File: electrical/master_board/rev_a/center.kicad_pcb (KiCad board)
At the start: 2 copper layers, 0 parts

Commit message: Inject the PCB outlines into master/center/ne/nw/se/sw PCB's.
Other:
- board outline added: 125 x 97.6 mm

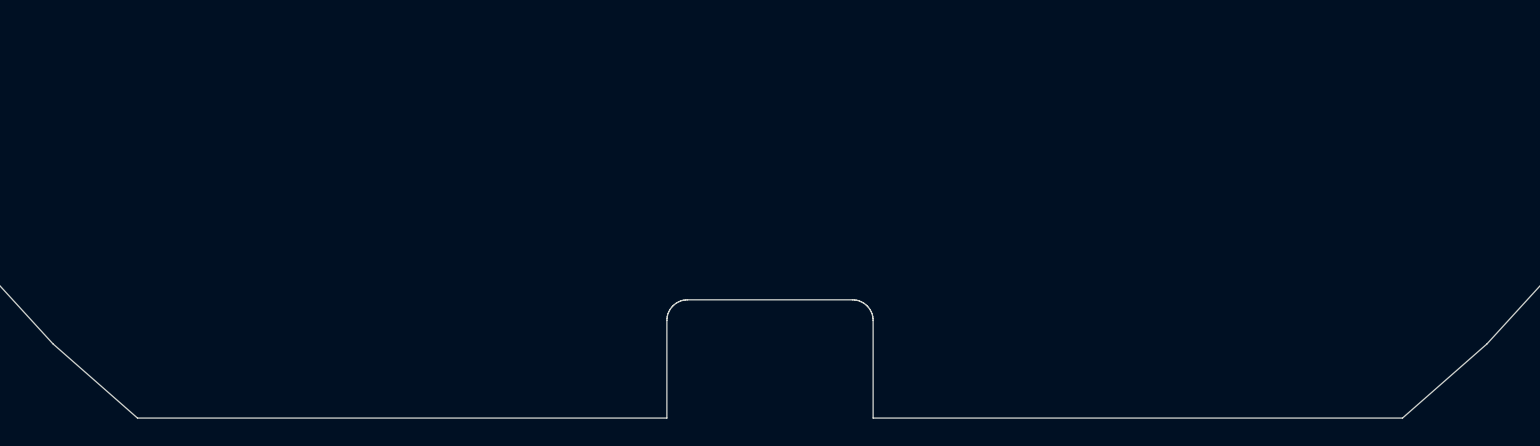
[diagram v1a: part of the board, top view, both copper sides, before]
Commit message: Updated some of the schematics and PCB's via hr2_models.py .
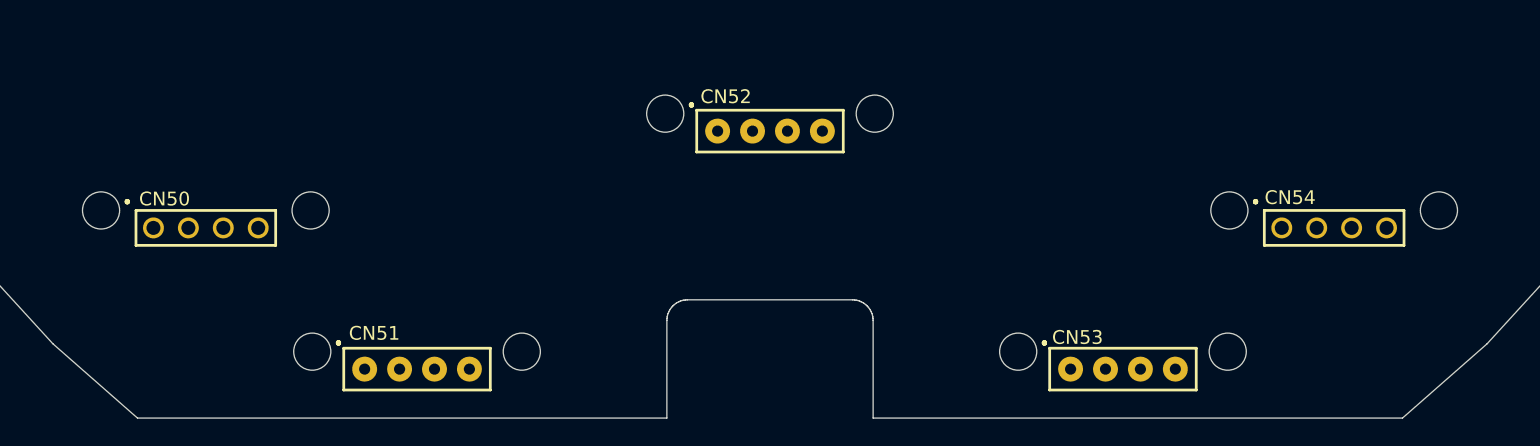
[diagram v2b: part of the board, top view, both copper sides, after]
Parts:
- added CN50: HCSR04;F1X4, HR2:HCSR04_F1x4_MATE, F.Cu at (59.0, 144.8)
- added CN51: HCSR04LP;F1X4, HR2:HCSR04_F1x4LP_MATE, F.Cu at (74.3, 155.0)
- added CN52: HCSR04LP;F1X4, HR2:HCSR04_F1x4LP_MATE, F.Cu at (100.0, 137.7)
- added CN53: HCSR04LP;F1X4, HR2:HCSR04_F1x4LP_MATE, F.Cu at (125.7, 155.0)
- added CN54: HCSR04;F1X4, HR2:HCSR04_F1x4_MATE, F.Cu at (141.0, 144.8)

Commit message: Successfully placed a font surface non-rotated footprint in ne.kicad_pcb.
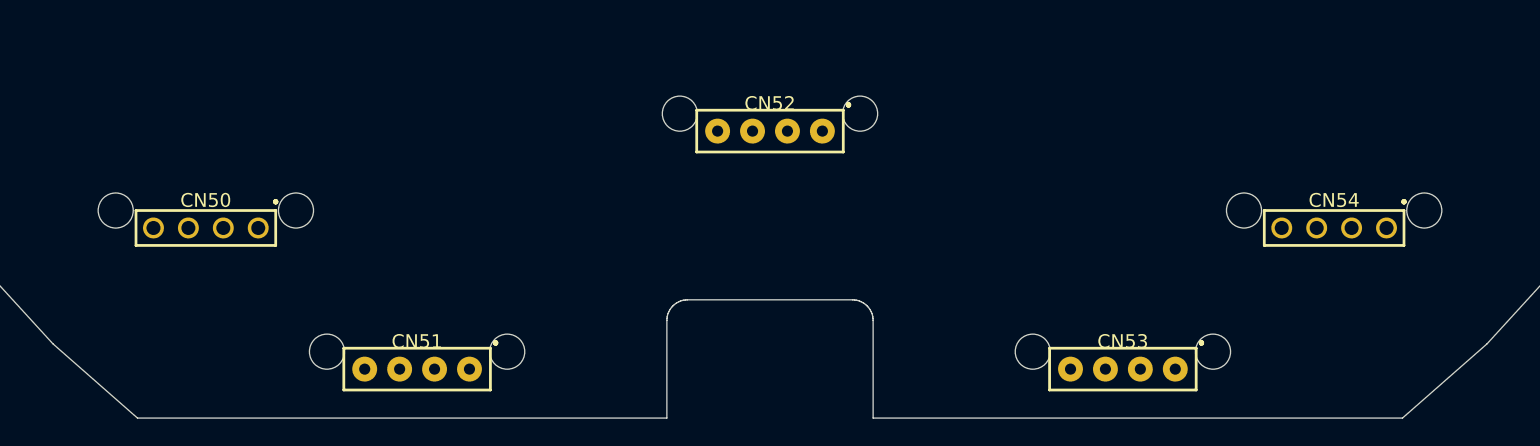
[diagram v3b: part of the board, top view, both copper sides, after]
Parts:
- CN50: value HCSR04;F1X4 -> HCSR04;F1x4; footprint HR2:HCSR04_F1x4_MATE -> HR2:HCSR04_F1x4
- CN51, CN53: value HCSR04LP;F1X4 -> HCSR04;F1x4LP; footprint HR2:HCSR04_F1x4LP_MATE -> HR2:HCSR04_F1x4LP; moved to B.Cu
- CN52: value HCSR04LP;F1X4 -> HCSR04;F1x4LP; footprint HR2:HCSR04_F1x4LP_MATE -> HR2:HCSR04_F1x4LP
- CN54: value HCSR04;F1X4 -> HCSR04;F1x4H; footprint HR2:HCSR04_F1x4_MATE -> HR2:HCSR04_F1x4H

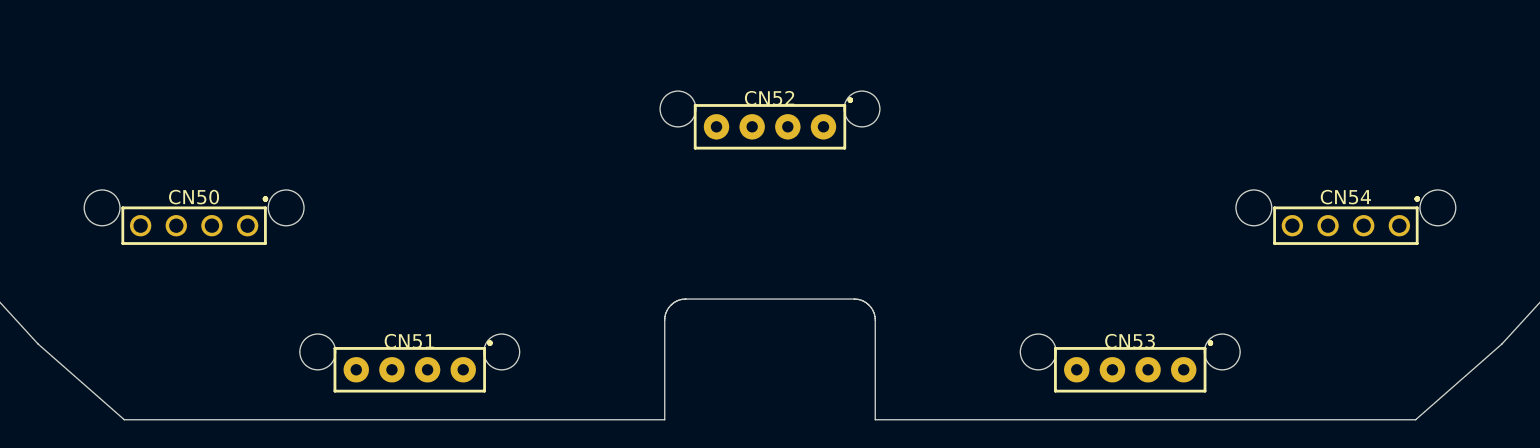
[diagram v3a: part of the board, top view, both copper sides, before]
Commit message: Finally sonars placed.  Had to manually specify the rotattions thought.
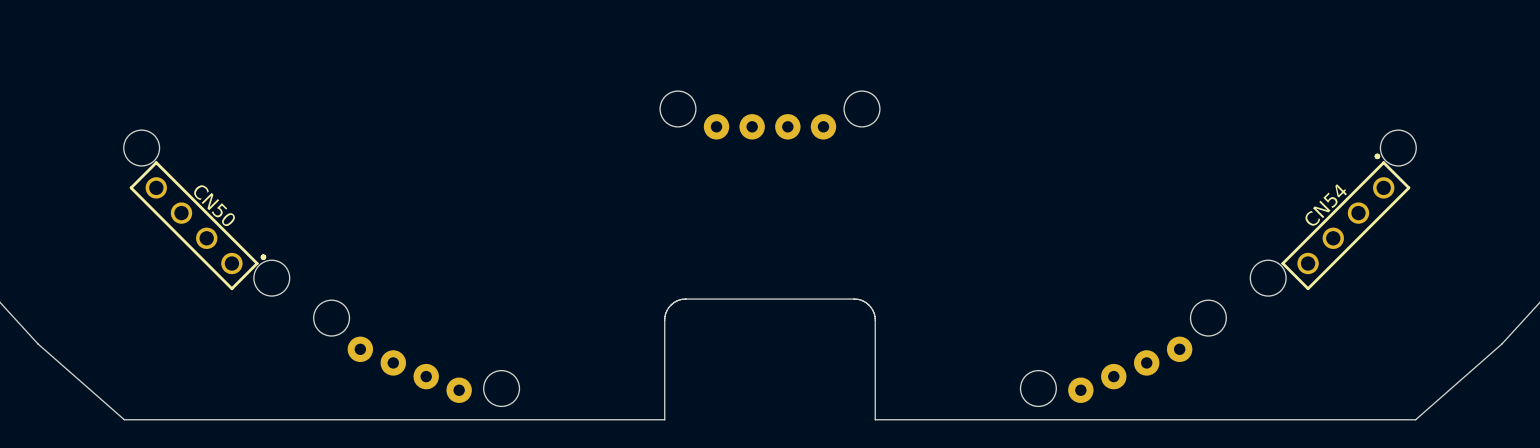
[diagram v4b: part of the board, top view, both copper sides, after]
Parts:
- CN52: moved to B.Cu
- turned CN50 to 315 degrees
- turned CN51 to 157.5 degrees
- turned CN52 to 180 degrees
- turned CN53 to 202.5 degrees
- turned CN54 to 45 degrees

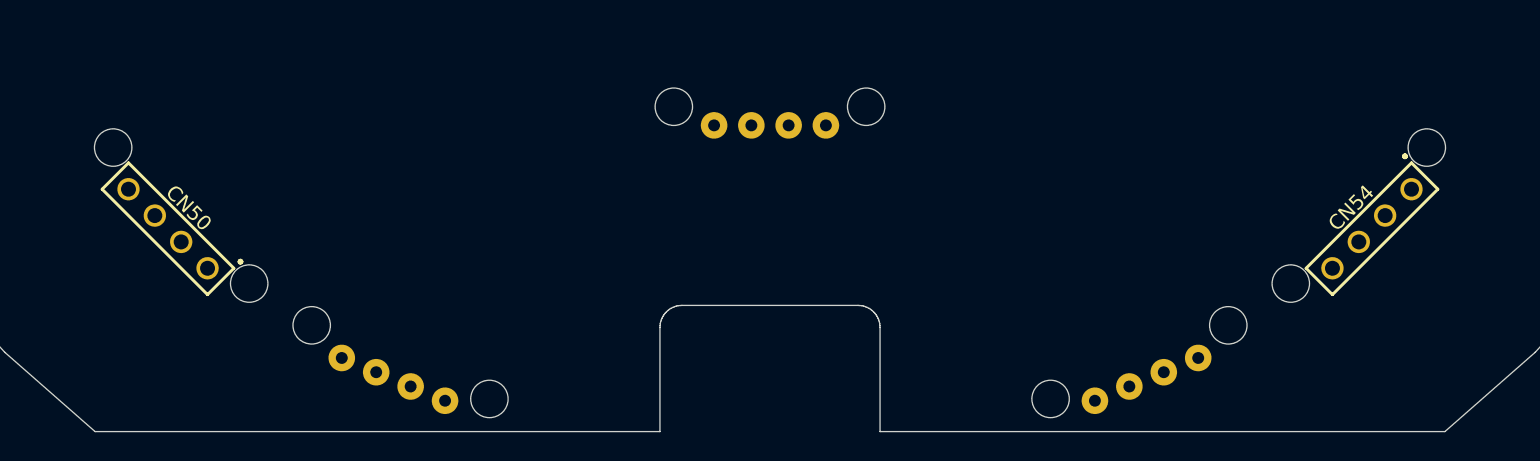
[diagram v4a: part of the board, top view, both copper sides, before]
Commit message: The PCBChunk'ification of Sonars is complete.
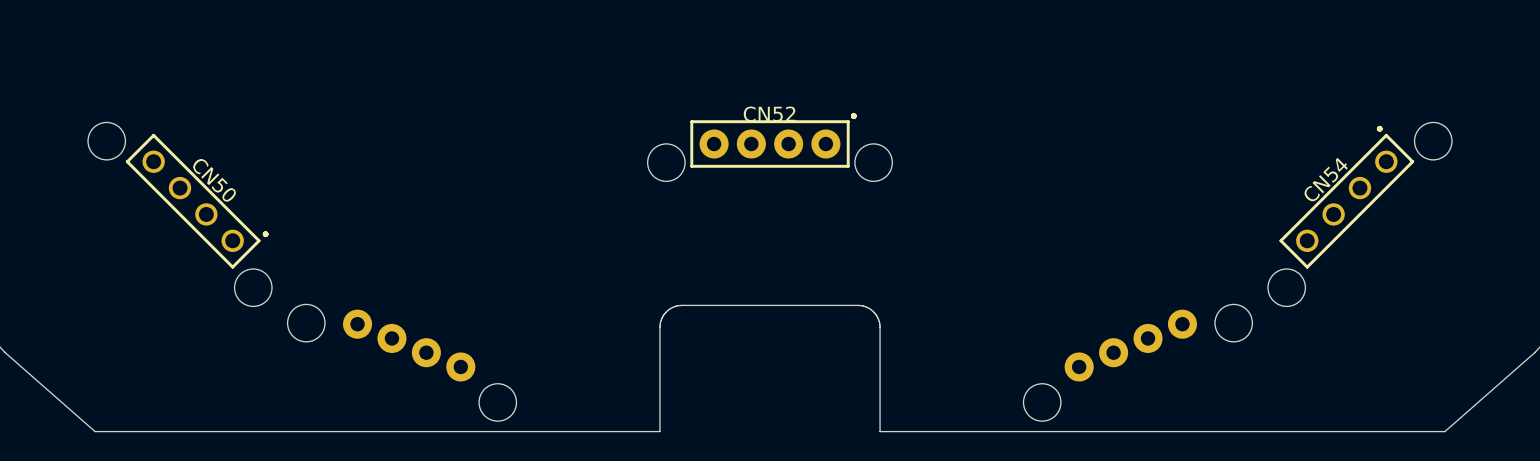
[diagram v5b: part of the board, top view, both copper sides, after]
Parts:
- CN50: value HCSR04;F1x4 -> HCSR04;F1X4
- CN51, CN53: value HCSR04;F1x4LP -> HCSR04LP;F1X4
- CN52: value HCSR04;F1x4LP -> HCSR04LP;F1X4; moved to F.Cu
- CN54: value HCSR04;F1x4H -> HCSR04;F1X4; footprint HR2:HCSR04_F1x4H -> HR2:HCSR04_F1x4
- moved CN54 2.54 mm to (139.3, 142.9)
- moved CN50 2.54 mm to (60.7, 142.9)
- moved CN51 2.54 mm to (75.4, 152.7)
- moved CN53 2.54 mm to (124.6, 152.7)
- moved CN52 1.27 mm to (100.0, 139.0), turned to 0 degrees

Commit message: Got Encoder PCB's installed on the center PCB.
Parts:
- added CN55: HR2_EncoderMate;2XF1X3, HR2:ENCODER_MATE, F.Cu at (136.0, 100.0)
- added CN56: HR2_EncoderMate;2XF1X3, HR2:ENCODER_MATE, F.Cu at (64.0, 100.0)
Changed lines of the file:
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@@
     (tracks 0)
     (zones 0)
-    (modules 5)
+    (modules 7)
     (nets 1)
   )
@@
     (add_net "Net-(CN54-Pad3)")
     (add_net "Net-(CN54-Pad4)")
+    (add_net "Net-(CN55-Pad1)")
+    (add_net "Net-(CN55-Pad2)")
+    (add_net "Net-(CN55-Pad3)")
+    (add_net "Net-(CN55-Pad4)")
+    (add_net "Net-(CN55-Pad5)")
+    (add_net "Net-(CN55-Pad6)")
+    (add_net "Net-(CN56-Pad1)")
+    (add_net "Net-(CN56-Pad2)")
+    (add_net "Net-(CN56-Pad3)")
+    (add_net "Net-(CN56-Pad4)")
+    (add_net "Net-(CN56-Pad5)")
+    (add_net "Net-(CN56-Pad6)")
+  )
+  (module HR2:ENCODER_MATE (layer F.Cu)
+    (at 136 100 180)
+    (fp_text reference CN55 (at 0 -2) (layer F.SilkS)
+      (effects (font (size 1 1) (thickness 0.2)))
+    )
+    (fp_text value HR2_EncoderMate;2XF1X3 (at 0 0) (layer F.Fab)
+      (effects (font (size 1 1) (thickness 0.2)))
+    )
+    (fp_line (start -1.27 -13.84) (end -1.27 -21.46) (layer F.SilkS) (width 0.2))
+    (fp_line (start 1.27 -13.84) (end -1.27 -13.84) (layer F.SilkS) (width 0.2))
+    (fp_line (start 1.27 -21.46) (end 1.27 -13.84) (layer F.SilkS) (width 0.2))
+    (fp_line (start -1.27 -21.46) (end 1.27 -21.46) (layer F.SilkS) (width 0.2))
+    (fp_line (start -1.83 -13.91) (end -1.91 -13.94) (layer F.SilkS) (width 0.2))
+    (fp_line (start -1.81 -13.84) (end -1.83 -13.91) (layer F.SilkS) (width 0.2))
+    (fp_line (start -1.83 -13.77) (end -1.81 -13.84) (layer F.SilkS) (width 0.2))
+    (fp_line (start -1.91 -13.74) (end -1.83 -13.77) (layer F.SilkS) (width 0.2))
+    (fp_line (start -1.98 -13.77) (end -1.91 -13.74) (layer F.SilkS) (width 0.2))
+    (fp_line (start -2.01 -13.84) (end -1.98 -13.77) (layer F.SilkS) (width 0.2))
+    (fp_line (start -1.98 -13.91) (end -2.01 -13.84) (layer F.SilkS) (width 0.2))
+    (fp_line (start -1.91 -13.94) (end -1.98 -13.91) (layer F.SilkS) (width 0.2))
+    (fp_line (start -1.27 21.46) (end -1.27 13.84) (layer F.SilkS) (width 0.2))
+    (fp_line (start 1.27 21.46) (end -1.27 21.46) (layer F.SilkS) (width 0.2))
+    (fp_line (start 1.27 13.84) (end 1.27 21.46) (layer F.SilkS) (width 0.2))
+    (fp_line (start -1.27 13.84) (end 1.27 13.84) (layer F.SilkS) (width 0.2))
+    (fp_line (start -1.83 21.39) (end -1.91 21.36) (layer F.SilkS) (width 0.2))
+    (fp_line (start -1.81 21.46) (end -1.83 21.39) (layer F.SilkS) (width 0.2))
+    (fp_line (start -1.83 21.53) (end -1.81 21.46) (layer F.SilkS) (width 0.2))
+    (fp_line (start -1.91 21.56) (end -1.83 21.53) (layer F.SilkS) (width 0.2))
+    (fp_line (start -1.98 21.53) (end -1.91 21.56) (layer F.SilkS) (width 0.2))
+    (fp_line (start -2.01 21.46) (end -1.98 21.53) (layer F.SilkS) (width 0.2))
+    (fp_line (start -1.98 21.39) (end -2.01 21.46) (layer F.SilkS) (width 0.2))
+    (fp_line (start -1.91 21.36) (end -1.98 21.39) (layer F.SilkS) (width 0.2))
+    (pad 3 thru_hole circle (at 0 15.11 180) (size 1.52 1.52) (drill 1.02) (layers *.Cu *.Mask))
+    (pad 2 thru_hole circle (at 0 17.65 180) (size 1.52 1.52) (drill 1.02) (layers *.Cu *.Mask))
+    (pad 1 thru_hole circle (at 0 20.19 180) (size 1.52 1.52) (drill 1.02) (layers *.Cu *.Mask))
+    (pad 6 thru_hole circle (at 0 -20.19 180) (size 1.52 1.52) (drill 1.02) (layers *.Cu *.Mask))
+    (pad 5 thru_hole circle (at 0 -17.65 180) (size 1.52 1.52) (drill 1.02) (layers *.Cu *.Mask))
+    (pad 4 thru_hole circle (at 0 -15.11 180) (size 1.52 1.52) (drill 1.02) (layers *.Cu *.Mask))
+  )
+  (module HR2:ENCODER_MATE (layer F.Cu)
+    (at 64 100)
+    (fp_text reference CN56 (at 0 -2) (layer F.SilkS)
+      (effects (font (size 1 1) (thickness 0.2)))
+    )
+    (fp_text value HR2_EncoderMate;2XF1X3 (at 0 0) (layer F.Fab)
+      (effects (font (size 1 1) (thickness 0.2)))
+    )
+    (fp_line (start -1.27 -13.84) (end -1.27 -21.46) (layer F.SilkS) (width 0.2))
+    (fp_line (start 1.27 -13.84) (end -1.27 -13.84) (layer F.SilkS) (width 0.2))
+    (fp_line (start 1.27 -21.46) (end 1.27 -13.84) (layer F.SilkS) (width 0.2))
+    (fp_line (start -1.27 -21.46) (end 1.27 -21.46) (layer F.SilkS) (width 0.2))
+    (fp_line (start -1.83 -13.91) (end -1.91 -13.94) (layer F.SilkS) (width 0.2))
+    (fp_line (start -1.81 -13.84) (end -1.83 -13.91) (layer F.SilkS) (width 0.2))
+    (fp_line (start -1.83 -13.77) (end -1.81 -13.84) (layer F.SilkS) (width 0.2))
+    (fp_line (start -1.91 -13.74) (end -1.83 -13.77) (layer F.SilkS) (width 0.2))
+    (fp_line (start -1.98 -13.77) (end -1.91 -13.74) (layer F.SilkS) (width 0.2))
+    (fp_line (start -2.01 -13.84) (end -1.98 -13.77) (layer F.SilkS) (width 0.2))
+    (fp_line (start -1.98 -13.91) (end -2.01 -13.84) (layer F.SilkS) (width 0.2))
+    (fp_line (start -1.91 -13.94) (end -1.98 -13.91) (layer F.SilkS) (width 0.2))
+    (fp_line (start -1.27 21.46) (end -1.27 13.84) (layer F.SilkS) (width 0.2))
+    (fp_line (start 1.27 21.46) (end -1.27 21.46) (layer F.SilkS) (width 0.2))
+    (fp_line (start 1.27 13.84) (end 1.27 21.46) (layer F.SilkS) (width 0.2))
+    (fp_line (start -1.27 13.84) (end 1.27 13.84) (layer F.SilkS) (width 0.2))
+    (fp_line (start -1.83 21.39) (end -1.91 21.36) (layer F.SilkS) (width 0.2))
+    (fp_line (start -1.81 21.46) (end -1.83 21.39) (layer F.SilkS) (width 0.2))
+    (fp_line (start -1.83 21.53) (end -1.81 21.46) (layer F.SilkS) (width 0.2))
+    (fp_line (start -1.91 21.56) (end -1.83 21.53) (layer F.SilkS) (width 0.2))
+    (fp_line (start -1.98 21.53) (end -1.91 21.56) (layer F.SilkS) (width 0.2))
+    (fp_line (start -2.01 21.46) (end -1.98 21.53) (layer F.SilkS) (width 0.2))
+    (fp_line (start -1.98 21.39) (end -2.01 21.46) (layer F.SilkS) (width 0.2))
+    (fp_line (start -1.91 21.36) (end -1.98 21.39) (layer F.SilkS) (width 0.2))
+    (pad 3 thru_hole circle (at 0 15.11) (size 1.52 1.52) (drill 1.02) (layers *.Cu *.Mask))
+    (pad 2 thru_hole circle (at 0 17.65) (size 1.52 1.52) (drill 1.02) (layers *.Cu *.Mask))
+    (pad 1 thru_hole circle (at 0 20.19) (size 1.52 1.52) (drill 1.02) (layers *.Cu *.Mask))
+    (pad 6 thru_hole circle (at 0 -20.19) (size 1.52 1.52) (drill 1.02) (layers *.Cu *.Mask))
+    (pad 5 thru_hole circle (at 0 -17.65) (size 1.52 1.52) (drill 1.02) (layers *.Cu *.Mask))
+    (pad 4 thru_hole circle (at 0 -15.11) (size 1.52 1.52) (drill 1.02) (layers *.Cu *.Mask))
   )
   (module HR2:HCSR04_F1x4LP (layer B.Cu)
